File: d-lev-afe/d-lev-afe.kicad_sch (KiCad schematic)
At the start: 28 parts, among them J1 S8B-PH-SM4-TB, Q1 MMBT3904, Q2 MMBT3906, U1 74AHC04, U3 SRV05-4, U4 AP2112K-3.3

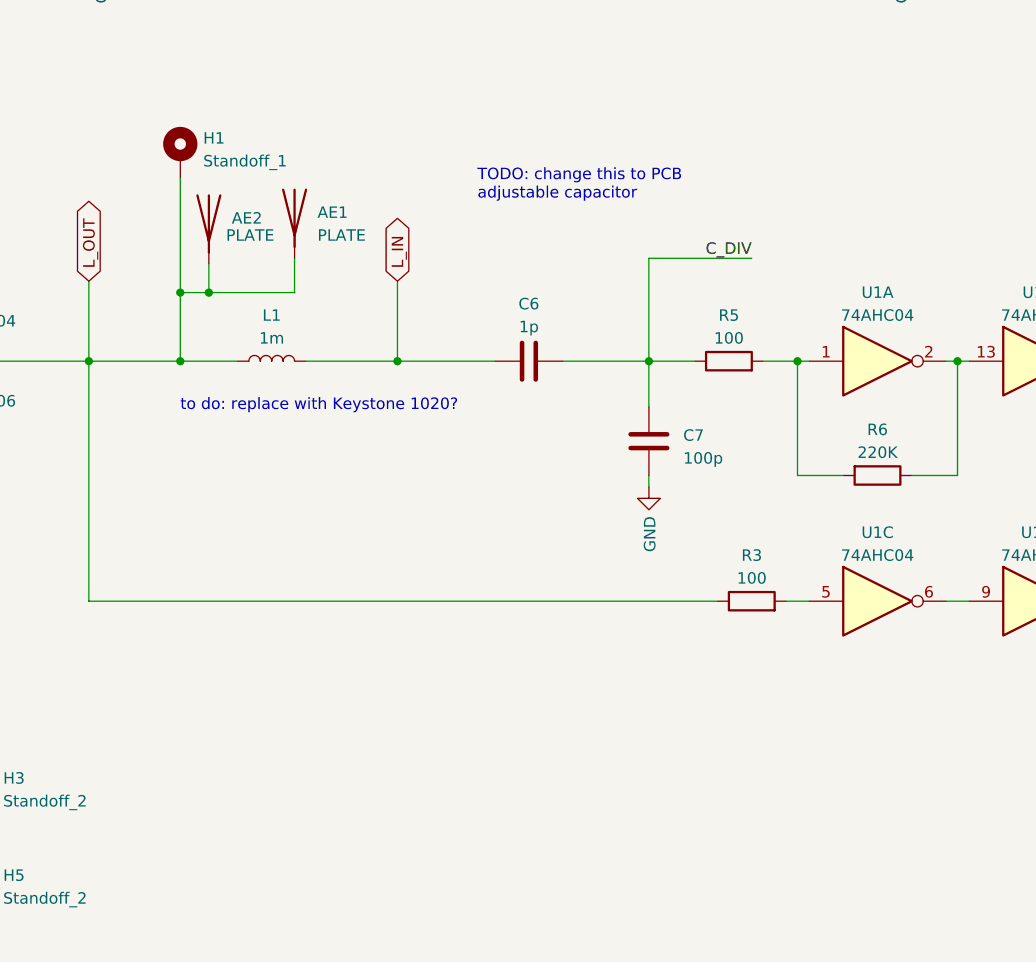
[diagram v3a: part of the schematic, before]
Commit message: Aesthetic improvements to main/AFE
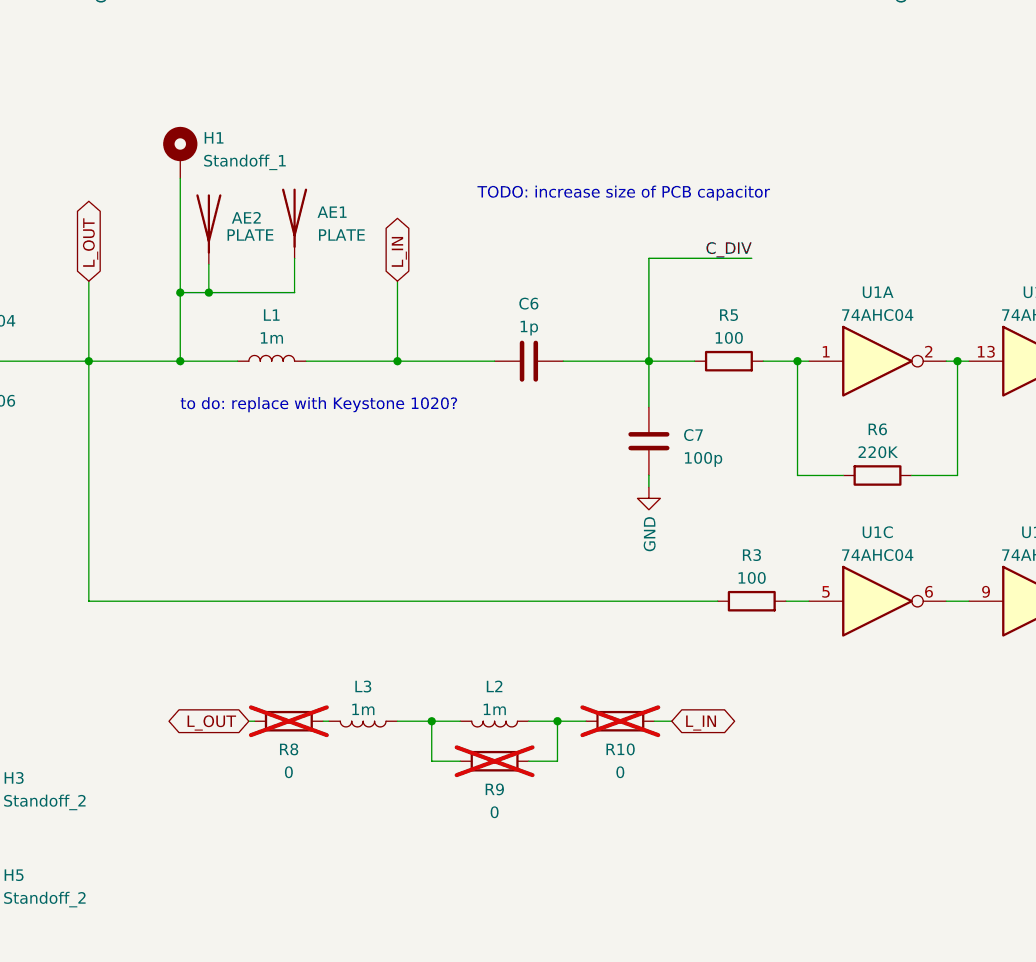
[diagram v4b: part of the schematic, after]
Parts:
- added L2, L3: 1m, theremin:Coilcraft_DO1605T, symbol Device:L
- added R10, R8, R9: 0, Resistor_SMD:R_0603_1608Metric, symbol Device:R
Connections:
- net L_IN: now also R10.1
- net L_OUT: now also R8.2
- new net: L2.1, R10.2, R9.1
- new net: L2.2, L3.1, R9.2
- new net: L3.2, R8.1
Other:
- note added: "TODO: increase size of PCB capacitor"
- note removed: "TODO: change this to PCB adjustable capacitor"
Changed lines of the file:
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@@
   (junction (at 170.18 111.76) (diameter 0) (color 0 0 0 0)
   )
+  (junction (at 146.05 151.765) (diameter 0) (color 0 0 0 0)
+  )
   (junction (at 34.29 46.99) (diameter 0) (color 0 0 0 0)
   )
@@
   )
   (junction (at 121.285 104.14) (diameter 0) (color 0 0 0 0)
+  )
+  (junction (at 160.02 151.765) (diameter 0) (color 0 0 0 0)
   )
   (junction (at 107.95 111.76) (diameter 0) (color 0 0 0 0)
@@
     (stroke (width 0) (type default))
   )
+  (wire (pts (xy 156.845 156.21) (xy 160.02 156.21))
+    (stroke (width 0) (type default))
+  )
+  (wire (pts (xy 146.05 156.21) (xy 146.05 151.765))
+    (stroke (width 0) (type default))
+  )
   (wire (pts (xy 78.74 113.03) (xy 78.74 118.11))
     (stroke (width 0) (type default))
@@
     (stroke (width 0) (type default))
   )
+  (wire (pts (xy 146.05 151.765) (xy 149.225 151.765))
+    (stroke (width 0) (type default))
+  )
   (wire (pts (xy 160.655 111.76) (xy 170.18 111.76))
     (stroke (width 0) (type default))
@@
     (stroke (width 0) (type default))
   )
+  (wire (pts (xy 146.05 156.21) (xy 149.225 156.21))
+    (stroke (width 0) (type default))
+  )
   (wire (pts (xy 186.69 111.76) (xy 186.69 124.46))
     (stroke (width 0) (type default))
@@
     (stroke (width 0) (type default))
   )
+  (wire (pts (xy 170.815 151.765) (xy 172.72 151.765))
+    (stroke (width 0) (type default))
+  )
   (wire (pts (xy 46.99 57.15) (xy 46.99 66.675))
     (stroke (width 0) (type default))
@@
     (stroke (width 0) (type default))
   )
+  (wire (pts (xy 125.73 151.765) (xy 126.365 151.765))
+    (stroke (width 0) (type default))
+  )
   (wire (pts (xy 78.74 105.41) (xy 78.74 113.03))
     (stroke (width 0) (type default))
@@
     (stroke (width 0) (type default))
   )
+  (wire (pts (xy 160.02 156.21) (xy 160.02 151.765))
+    (stroke (width 0) (type default))
+  )
   (wire (pts (xy 59.69 53.975) (xy 59.69 46.99))
     (stroke (width 0) (type default))
@@
     (stroke (width 0) (type default))
   )
+  (wire (pts (xy 160.02 151.765) (xy 156.845 151.765))
+    (stroke (width 0) (type default))
+  )
   (wire (pts (xy 165.862 54.61) (xy 170.942 54.61))
     (stroke (width 0) (type default))
@@
     (stroke (width 0) (type default))
   )
+  (wire (pts (xy 142.24 151.765) (xy 146.05 151.765))
+    (stroke (width 0) (type default))
+  )
   (wire (pts (xy 87.63 97.79) (xy 87.63 100.33))
     (stroke (width 0) (type default))
   )
+  (wire (pts (xy 160.02 151.765) (xy 163.195 151.765))
+    (stroke (width 0) (type default))
+  )
   (wire (pts (xy 59.69 61.595) (xy 59.69 64.77))
     (stroke (width 0) (type default))
   )
   (wire (pts (xy 109.22 57.15) (xy 109.22 64.77))
+    (stroke (width 0) (type default))
+  )
+  (wire (pts (xy 133.985 151.765) (xy 134.62 151.765))
     (stroke (width 0) (type default))
   )
@@
     (effects (font (size 1.27 1.27)) (justify left bottom))
   )
-  (text "TODO: change this to PCB \nadjustable capacitor" (at 151.13 93.98 0)
+  (text "TODO: increase size of PCB capacitor" (at 151.13 93.98 0)
     (effects (font (size 1.27 1.27)) (justify left bottom))
   )
@@
     )
   )
+  (global_label "L_OUT" (shape bidirectional) (at 125.73 151.765 180) (fields_autoplaced)
+    (effects (font (size 1.27 1.27)) (justify right))
+    (property "Intersheetrefs" "${INTERSHEET_REFS}" (at 116.0886 151.765 0)
+      (effects (font (size 1.27 1.27)) (justify right) hide)
+    )
+  )
   (global_label "L_OUT" (shape bidirectional) (at 222.25 45.72 0) (fields_autoplaced)
     (effects (font (size 1.27 1.27)) (justify left))
@@
     )
   )
+  (global_label "L_IN" (shape bidirectional) (at 172.72 151.765 0) (fields_autoplaced)
+    (effects (font (size 1.27 1.27)) (justify left))
+    (property "Intersheetrefs" "${INTERSHEET_REFS}" (at 180.6681 151.765 0)
+      (effects (font (size 1.27 1.27)) (justify left) hide)
+    )
+  )
   (global_label "SQ" (shape output) (at 40.64 113.03 180) (fields_autoplaced)
     (effects (font (size 1.27 1.27)) (justify right))
@@
         (path "/3b0ead2a-6fae-4ae2-8192-98c9e26989ec"
           (reference "C2") (unit 1)
+        )
+      )
+    )
+  )
+  (symbol (lib_id "Device:R") (at 153.035 156.21 270) (unit 1)
+    (in_bom yes) (on_board yes) (dnp yes) (fields_autoplaced)
+    (property "Reference" "R9" (at 153.035 159.385 90)
+      (effects (font (size 1.27 1.27)))
+    )
+    (property "Value" "0" (at 153.035 161.925 90)
+      (effects (font (size 1.27 1.27)))
+    )
+    (property "Footprint" "Resistor_SMD:R_0603_1608Metric" (at 153.035 154.432 90)
+      (effects (font (size 1.27 1.27)) hide)
+    )
+    (property "Datasheet" "~" (at 153.035 156.21 0)
+      (effects (font (size 1.27 1.27)) hide)
+    )
+    (pin "1")
+    (pin "2")
+    (instances
+      (project "d-lev-afe"
+        (path "/3b0ead2a-6fae-4ae2-8192-98c9e26989ec"
+          (reference "R9") (unit 1)
         )
       )
@@
     )
   )
+  (symbol (lib_id "Device:L") (at 138.43 151.765 270) (unit 1)
+    (in_bom no) (on_board yes) (dnp no) (fields_autoplaced)
+    (property "Reference" "L3" (at 138.43 147.955 90)
+      (effects (font (size 1.27 1.27)))
+    )
+    (property "Value" "1m" (at 138.43 150.495 90)
+      (effects (font (size 1.27 1.27)))
+    )
+    (property "Footprint" "theremin:Coilcraft_DO1605T" (at 138.43 151.765 0)
+      (effects (font (size 1.27 1.27)) hide)
+    )
+    (property "Datasheet" "~" (at 138.43 151.765 0)
+      (effects (font (size 1.27 1.27)) hide)
+    )
+    (pin "1")
+    (pin "2")
+    (instances
+      (project "d-lev-afe"
+        (path "/3b0ead2a-6fae-4ae2-8192-98c9e26989ec"
+          (reference "L3") (unit 1)
+        )
+      )
+    )
+  )
   (symbol (lib_id "power:+3V3") (at 72.39 123.19 0) (unit 1)
     (in_bom yes) (on_board yes) (dnp no)
@@
         (path "/3b0ead2a-6fae-4ae2-8192-98c9e26989ec"
           (reference "#PWR07") (unit 1)
+        )
+      )
+    )
+  )
+  (symbol (lib_id "Device:R") (at 167.005 151.765 270) (unit 1)
+    (in_bom yes) (on_board yes) (dnp yes) (fields_autoplaced)
+    (property "Reference" "R10" (at 167.005 154.94 90)
+      (effects (font (size 1.27 1.27)))
+    )
+    (property "Value" "0" (at 167.005 157.48 90)
+      (effects (font (size 1.27 1.27)))
+    )
+    (property "Footprint" "Resistor_SMD:R_0603_1608Metric" (at 167.005 149.987 90)
+      (effects (font (size 1.27 1.27)) hide)
+    )
+    (property "Datasheet" "~" (at 167.005 151.765 0)
+      (effects (font (size 1.27 1.27)) hide)
+    )
+    (pin "1")
+    (pin "2")
+    (instances
+      (project "d-lev-afe"
+        (path "/3b0ead2a-6fae-4ae2-8192-98c9e26989ec"
+          (reference "R10") (unit 1)
         )
       )
@@
     )
   )
+  (symbol (lib_id "Device:L") (at 153.035 151.765 270) (unit 1)
+    (in_bom no) (on_board yes) (dnp no) (fields_autoplaced)
+    (property "Reference" "L2" (at 153.035 147.955 90)
+      (effects (font (size 1.27 1.27)))
+    )
+    (property "Value" "1m" (at 153.035 150.495 90)
+      (effects (font (size 1.27 1.27)))
+    )
+    (property "Footprint" "theremin:Coilcraft_DO1605T" (at 153.035 151.765 0)
+      (effects (font (size 1.27 1.27)) hide)
+    )
+    (property "Datasheet" "~" (at 153.035 151.765 0)
+      (effects (font (size 1.27 1.27)) hide)
+    )
+    (pin "1")
+    (pin "2")
+    (instances
+      (project "d-lev-afe"
+        (path "/3b0ead2a-6fae-4ae2-8192-98c9e26989ec"
+          (reference "L2") (unit 1)
+        )
+      )
+    )
+  )
   (symbol (lib_id "74xx:74AHC04") (at 195.58 111.76 0) (unit 1)
     (in_bom yes) (on_board yes) (dnp no) (fields_autoplaced)
@@
         )
       )
+    )
+  )
+  (symbol (lib_id "Device:R") (at 130.175 151.765 270) (unit 1)
+    (in_bom yes) (on_board yes) (dnp yes) (fields_autoplaced)
+    (property "Reference" "R8" (at 130.175 154.94 90)
+      (effects (font (size 1.27 1.27)))
+    )
+    (property "Value" "0" (at 130.175 157.48 90)
+      (effects (font (size 1.27 1.27)))
+    )
+    (property "Footprint" "Resistor_SMD:R_0603_1608Metric" (at 130.175 149.987 90)
+      (effects (font (size 1.27 1.27)) hide)
+    )
+    (property "Datasheet" "~" (at 130.175 151.765 0)
+      (effects (font (size 1.27 1.27)) hide)
+    )
+    (pin "1")
+    (pin "2")
+    (instances
+      (project "d-lev-afe"
+        (path "/3b0ead2a-6fae-4ae2-8192-98c9e26989ec"
+          (reference "R8") (unit 1)
+        )
+      )

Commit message: more routing
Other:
- note added: "TODO: increase size of PCB capacitor Replace with a normal capacitor"
- note removed: "TODO: increase size of PCB capacitor"
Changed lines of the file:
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@@
     (effects (font (size 1.27 1.27)) (justify left bottom))
   )
-  (text "TODO: increase size of PCB capacitor" (at 151.13 93.98 0)
+  (text "TODO: increase size of PCB capacitor\nReplace with a normal capacitor"
+    (at 151.13 93.98 0)
     (effects (font (size 1.27 1.27)) (justify left bottom))
   )

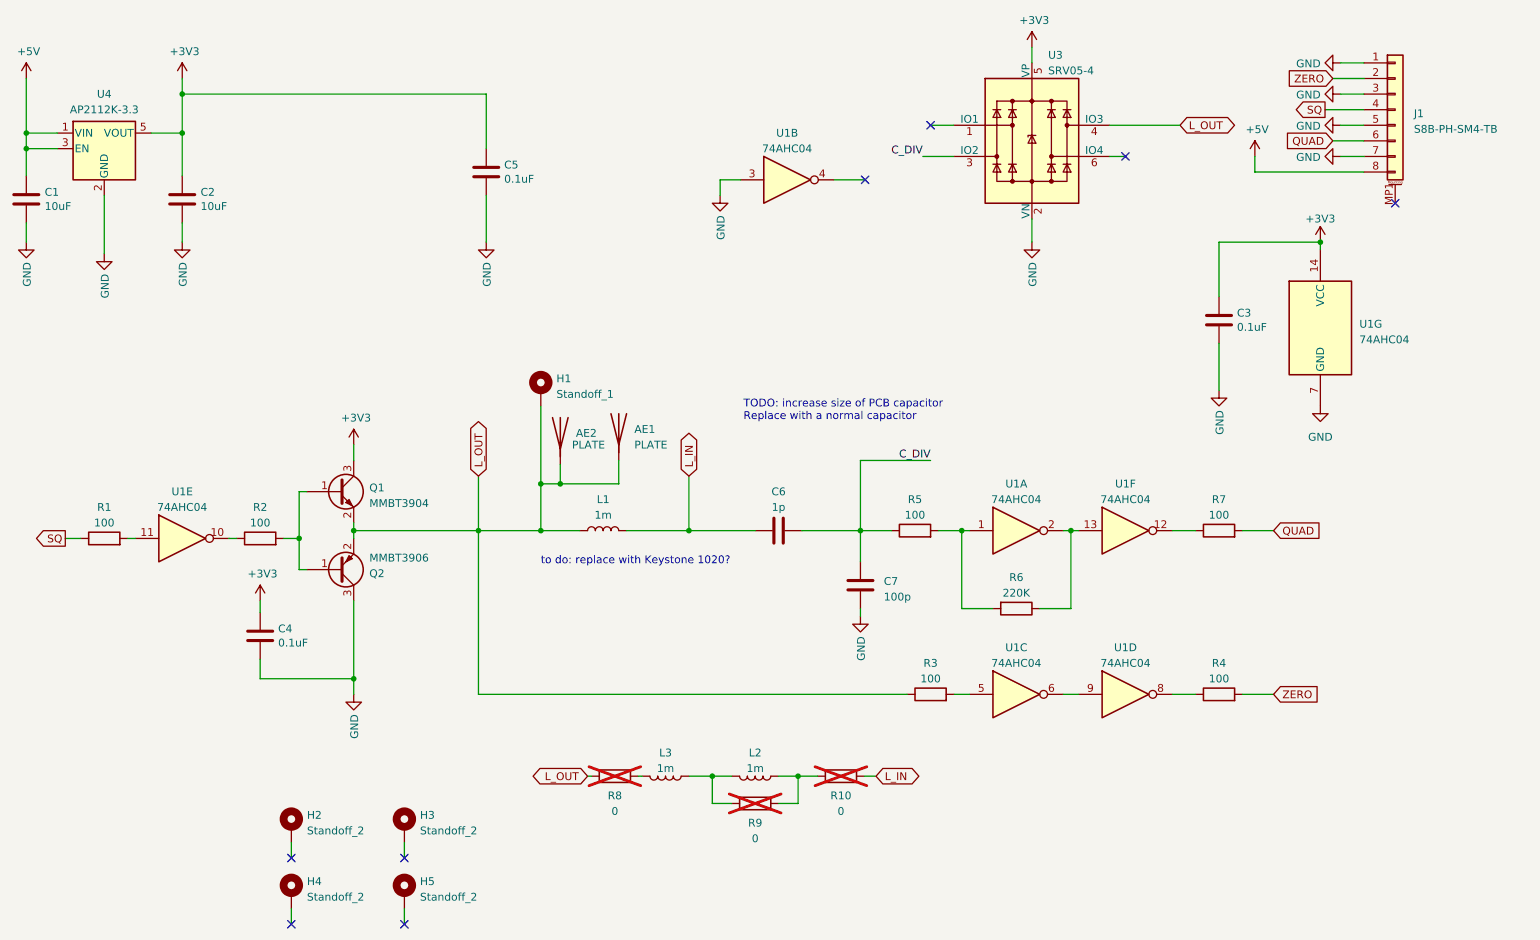
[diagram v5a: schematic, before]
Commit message: d-lev-afe: de-rounded traces
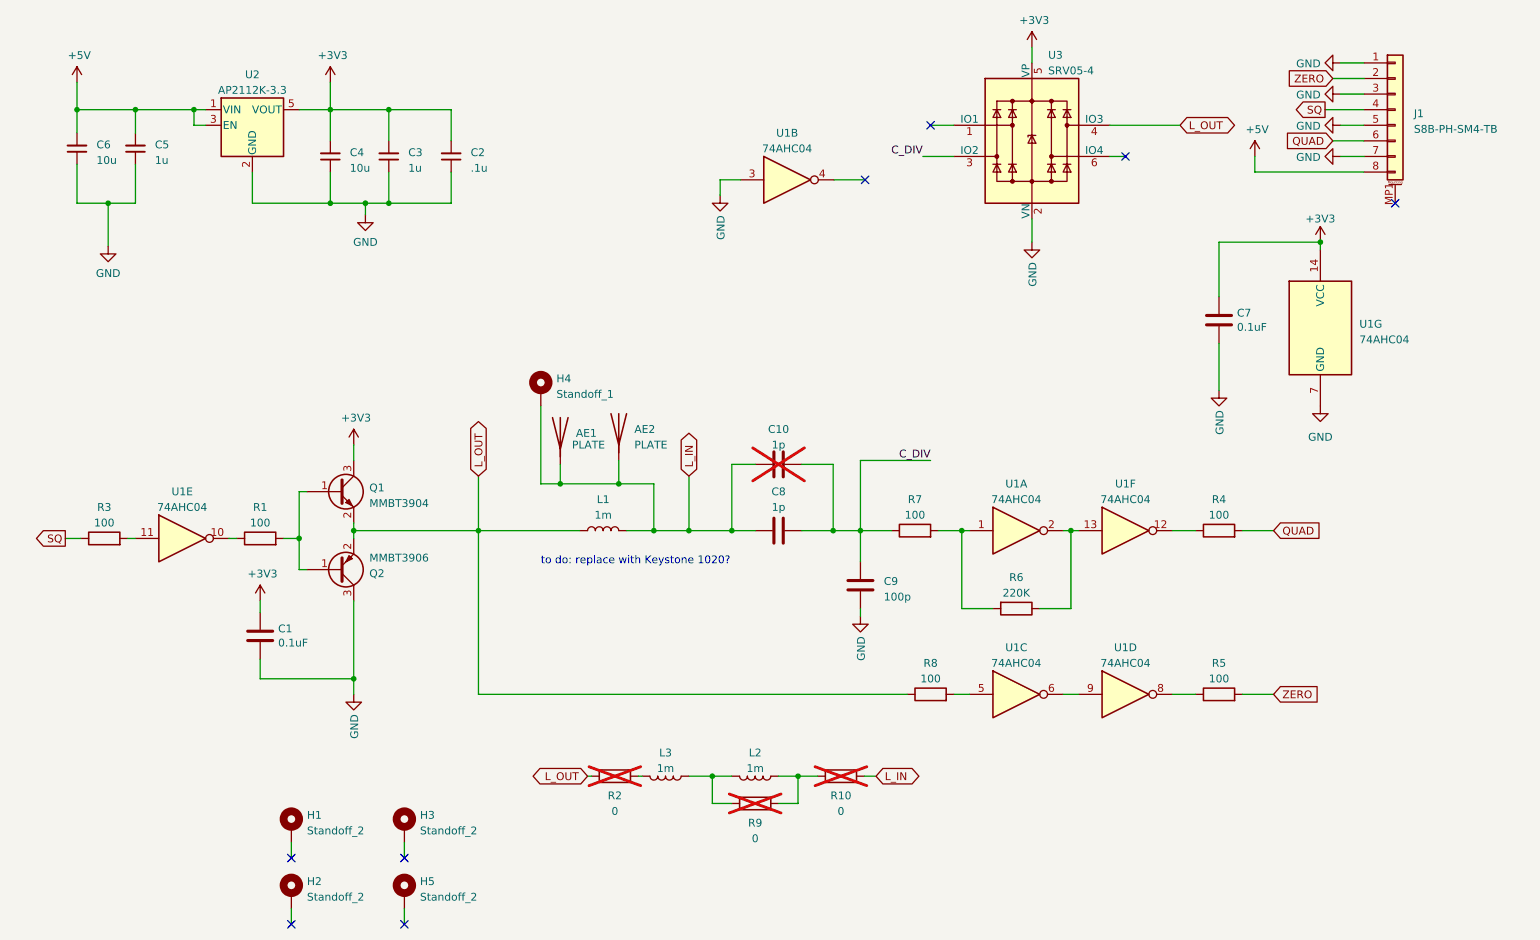
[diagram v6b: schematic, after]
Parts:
- removed C1, C2: 10uF, Capacitor_SMD:C_0603_1608Metric, symbol Device:C
- removed C5: 0.1uF, Capacitor_SMD:C_0603_1608Metric, symbol Device:C
- removed U4: AP2112K-3.3, Package_TO_SOT_SMD:SOT-23-5, symbol Regulator_Linear:AP2112K-3.3
- added C10: 1p, Capacitor_SMD:C_0805_2012Metric_Pad1.18x1.45mm_HandSolder, symbol Device:C
- added C2: .1u, Capacitor_SMD:C_0603_1608Metric, symbol Device:C_Small
- added C3, C5: 1u, Capacitor_SMD:C_0603_1608Metric, symbol Device:C_Small
- added C4, C6: 10u, Capacitor_SMD:C_0805_2012Metric, symbol Device:C_Small
- added U2: AP2112K-3.3, Package_TO_SOT_SMD:SOT-23-5, symbol Regulator_Linear:AP2112K-3.3
- C8: renamed from C6; footprint theremin:testpoint_cap_1pf -> Capacitor_SMD:C_0805_2012Metric_Pad1.18x1.45mm_HandSolder
- H1: renamed from H2; footprint theremin:SMTSO-M4 -> theremin:SMTSO-M3
- H2: renamed from H4; footprint theremin:SMTSO-M4 -> theremin:SMTSO-M3
- H3, H5: footprint theremin:SMTSO-M4 -> theremin:SMTSO-M3
- renumbered AE2 to AE1, AE1 to AE2, C4 to C1, C3 to C7, C7 to C9, H1 to H4, R2 to R1, R8 to R2, R1 to R3, R7 to R4, R4 to R5, R5 to R7, R3 to R8
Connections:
- net +3V3: now also C2.2, C3.2, C4.2, U2.5 (VOUT)
- net +5V: now also C5.2, C6.2, U2.1 (VIN), U2.3 (EN)
- net C_DIV: now also C10.2
- net GND: now also C2.1, C3.1, C4.1, C5.1, C6.1, U2.2 (GND)
- net L_IN: now also AE1.1 (A), AE2.1 (A), H4.1, C10.1
- net L_OUT: no longer AE1.1 (A), AE2.1 (A), H4.1
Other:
- note removed: "TODO: increase size of PCB capacitor Replace with a normal capacitor"
